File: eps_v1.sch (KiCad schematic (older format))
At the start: 5 parts

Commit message: Test commit
Wrote hello
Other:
- note added: "Hello"
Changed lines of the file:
@@
 Text HLabel 2350 7200 0    60   Input ~ 0
 -YI
+Text Notes 3450 3950 0    60   ~ 0
+Hello
 $EndSCHEMATC

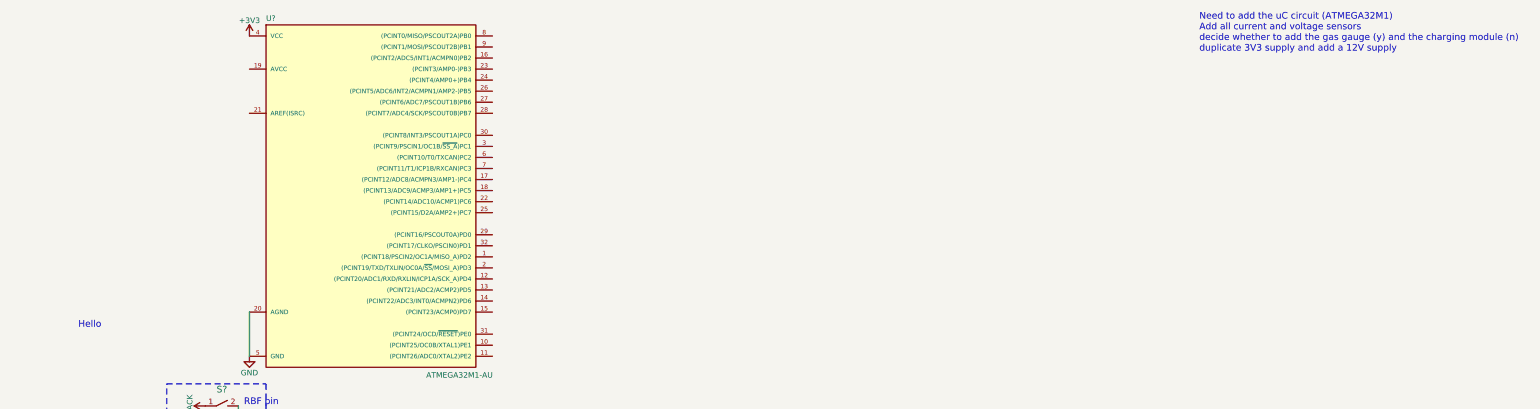
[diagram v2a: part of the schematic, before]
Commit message: Minor Edits
Took out a comment, edited other comments
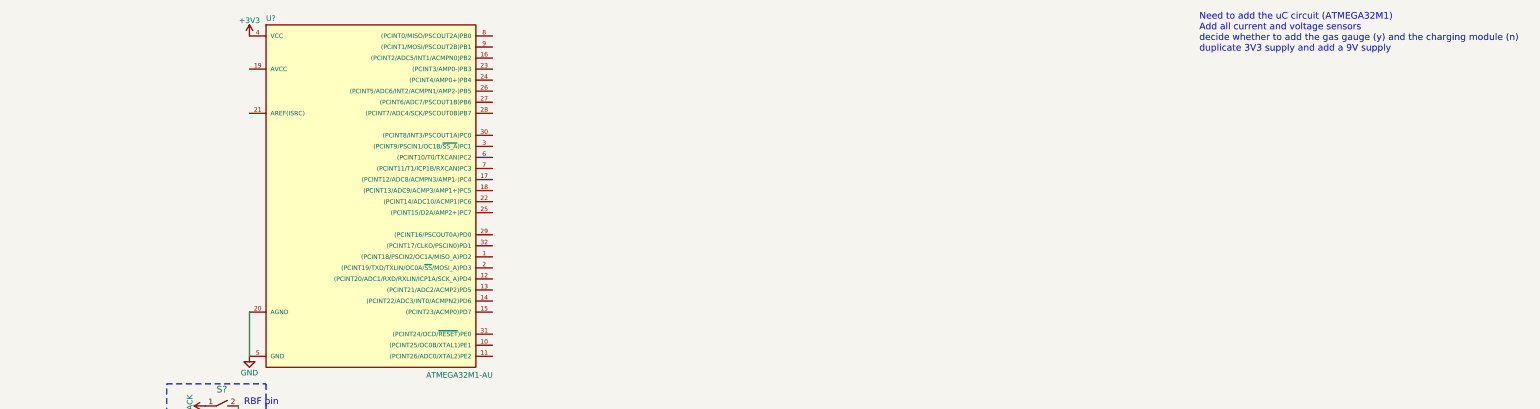
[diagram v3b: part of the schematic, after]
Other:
- note added: "Need to add the uC circuit (ATMEGA32M1)\nAdd all current and voltage sensors\ndecide whether to add the gas gauge (y) and the charging module (n)\nduplicate 3V3 supply and add a 9V supply"
- note removed: "Hello"
- note removed: "Need to add the uC circuit (ATMEGA32M1)\nAdd all current and voltage sensors\ndecide whether to add the gas gauge (y) and the charging module (n)\nduplicate 3V3 supply and add a 12V supply"
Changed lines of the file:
@@
 RBF pin
 Text Notes 13600 1450 0    60   ~ 0
-Need to add the uC circuit (ATMEGA32M1)\nAdd all current and voltage sensors\ndecide whether to add the gas gauge (y) and the charging module (n)\nduplicate 3V3 supply and add a 12V supply
+Need to add the uC circuit (ATMEGA32M1)\nAdd all current and voltage sensors\ndecide whether to add the gas gauge (y) and the charging module (n)\nduplicate 3V3 supply and add a 9V supply
 $Comp
 L ATMEGA32M1-AU U?
@@
 Text HLabel 2350 7200 0    60   Input ~ 0
 -YI
-Text Notes 3450 3950 0    60   ~ 0
-Hello
 $EndSCHEMATC
